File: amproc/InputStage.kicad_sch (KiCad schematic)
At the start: 19 parts

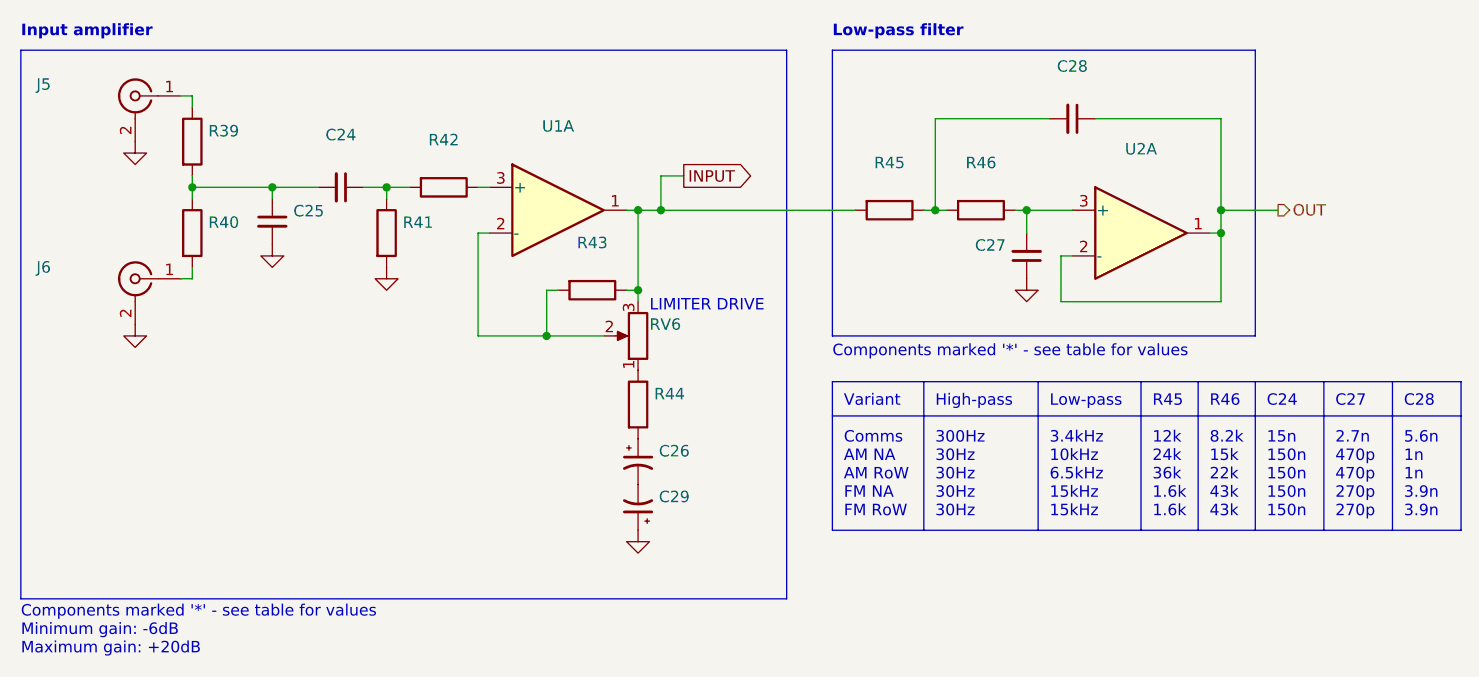
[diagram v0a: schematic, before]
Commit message: Fix U8, U9 pinouts
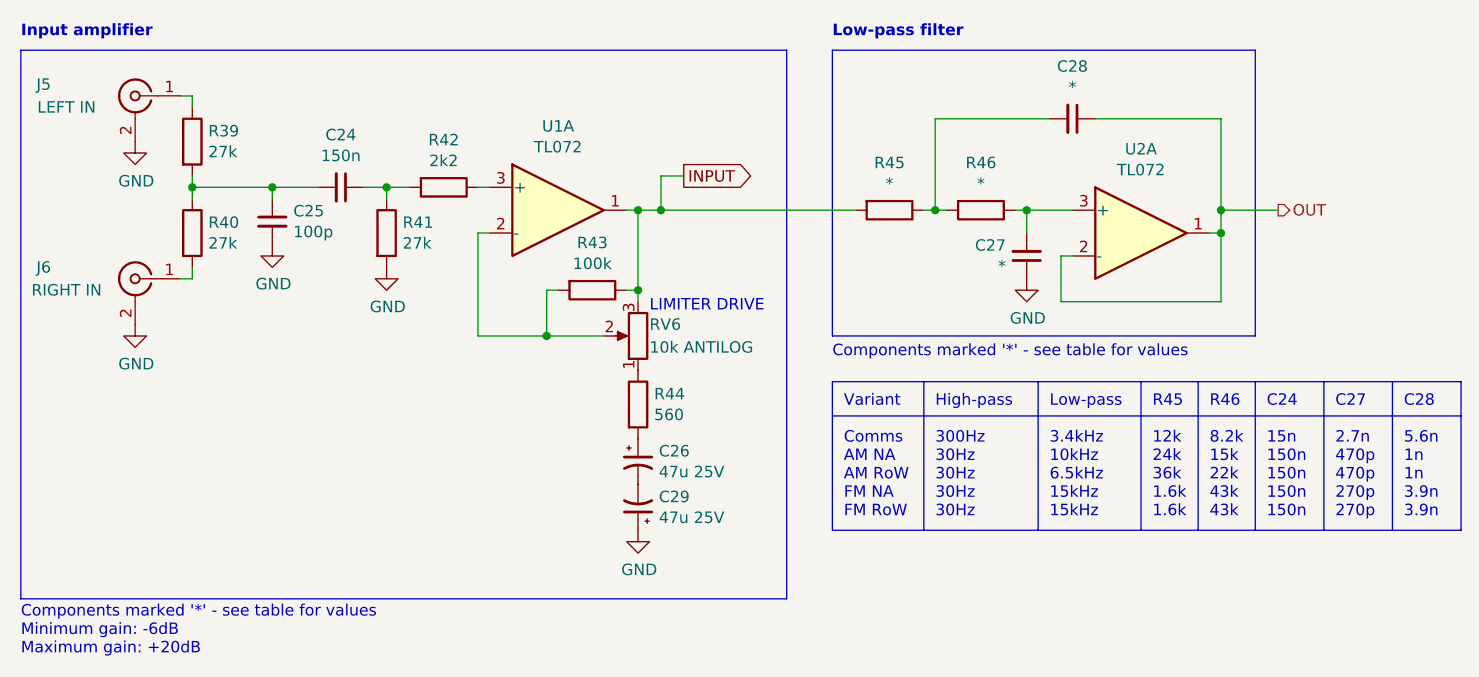
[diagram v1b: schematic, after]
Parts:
- C24: value (none) -> 150n; footprint (none) -> Capacitors_THT:C_Rect_L7.2mm_W2.5mm_P5.00mm_FKS2_FKP2_MKS2_MKP2
- C25: value (none) -> 100p; footprint (none) -> Capacitors_THT:C_Disc_D5.0mm_W2.5mm_P2.50mm
- C26, C29: value (none) -> 47u 25V; footprint (none) -> Capacitors_THT:CP_Radial_D5.0mm_P2.00mm
- C27, C28: value (none) -> *; footprint (none) -> Capacitors_THT:C_Rect_L7.2mm_W2.5mm_P5.00mm_FKS2_FKP2_MKS2_MKP2
- J5: value (none) -> LEFT IN; footprint (none) -> amproc:NYS354
- J6: value (none) -> RIGHT IN; footprint (none) -> amproc:NYS354
- R39, R40, R41: value (none) -> 27k; footprint (none) -> amproc:R_Axial_DIN0207_L6.3mm_D2.5mm_P7.62mm_Horizontal_FabText
- R42: value (none) -> 2k2; footprint (none) -> amproc:R_Axial_DIN0207_L6.3mm_D2.5mm_P7.62mm_Horizontal_FabText
- R43: value (none) -> 100k; footprint (none) -> amproc:R_Axial_DIN0207_L6.3mm_D2.5mm_P7.62mm_Horizontal_FabText
- R44: value (none) -> 560; footprint (none) -> amproc:R_Axial_DIN0207_L6.3mm_D2.5mm_P7.62mm_Horizontal_FabText
- R45, R46: value (none) -> *; footprint (none) -> amproc:R_Axial_DIN0207_L6.3mm_D2.5mm_P7.62mm_Horizontal_FabText
- RV6: value (none) -> 10k ANTILOG; footprint (none) -> amproc:PTD901-15K
- U1, U2: value (none) -> TL072; footprint (none) -> Housings_DIP:DIP-8_W7.62mm_LongPads
